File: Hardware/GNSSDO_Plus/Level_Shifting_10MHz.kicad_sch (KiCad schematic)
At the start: 57 parts, among them J10 SMA_Edge, J8 SMA_Edge, U15 SN74LVC1G175DCK, U17 LMV7219M5, U20 LMV7219M5, U23 LMV7219M5, U24 LMV7219M5

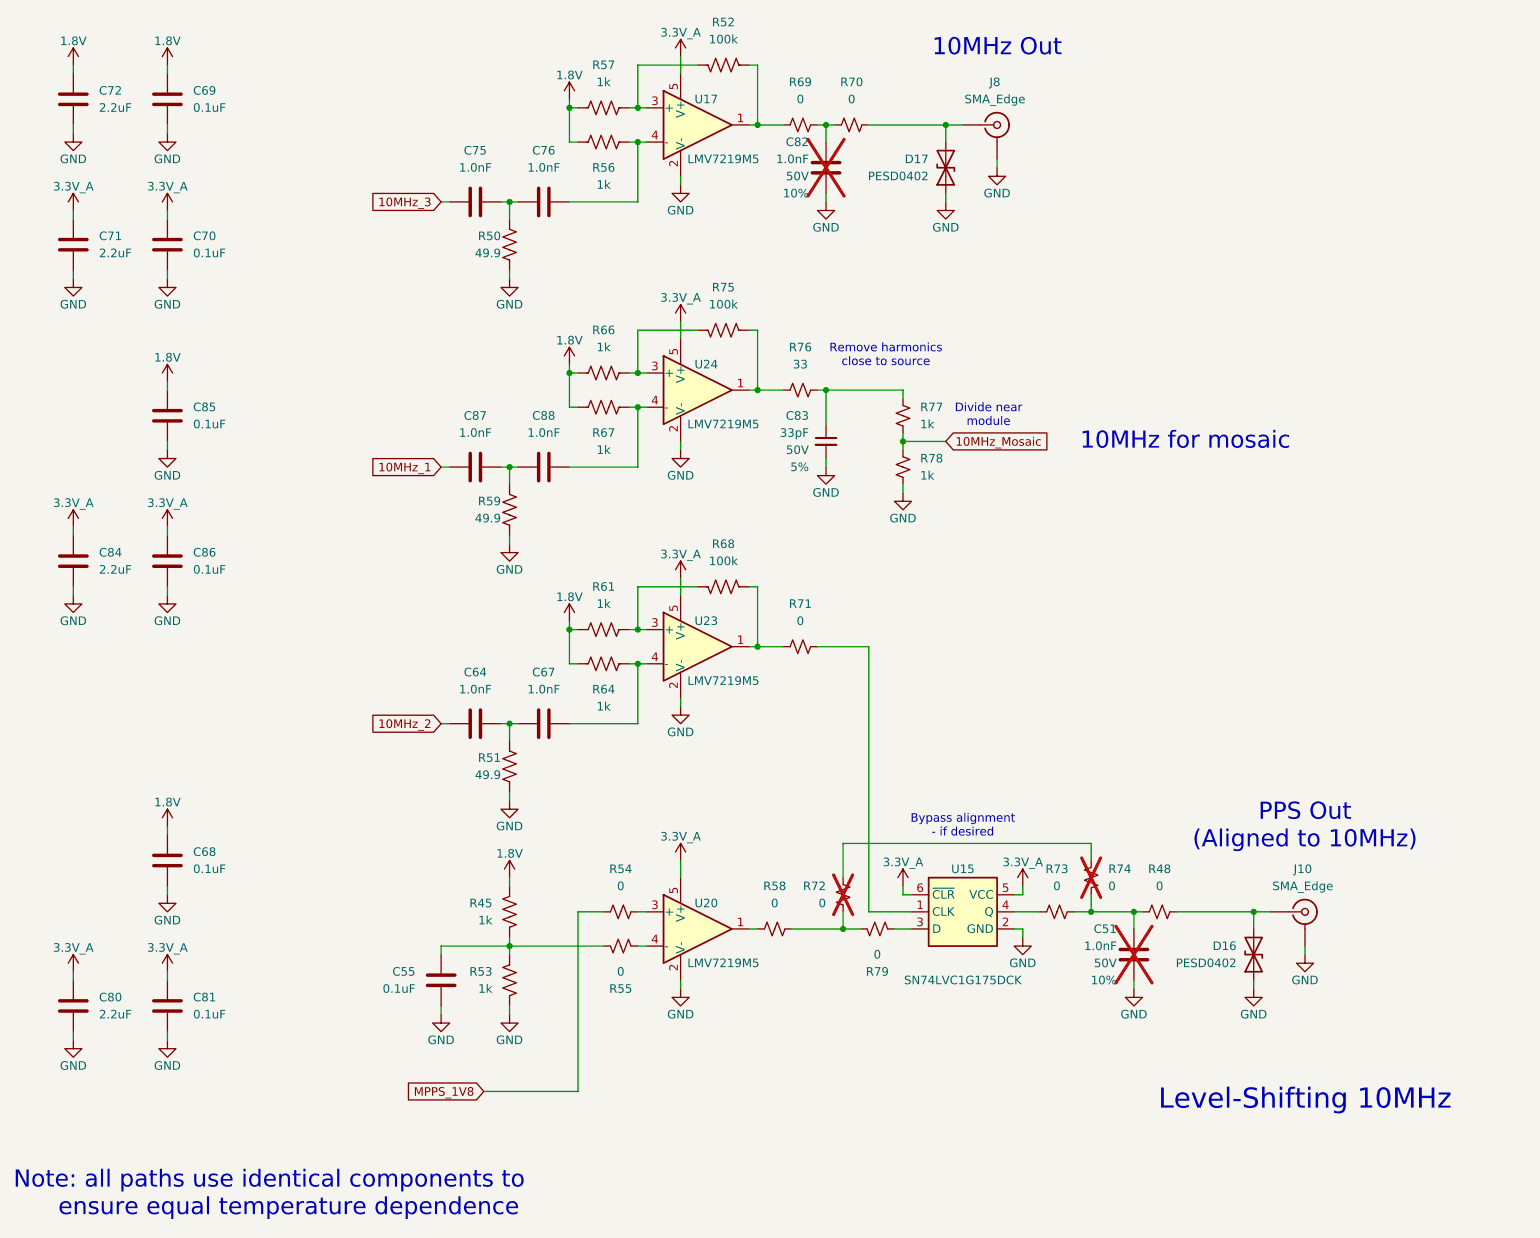
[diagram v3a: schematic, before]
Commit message: GNSSDO+ : update symbols and footprints
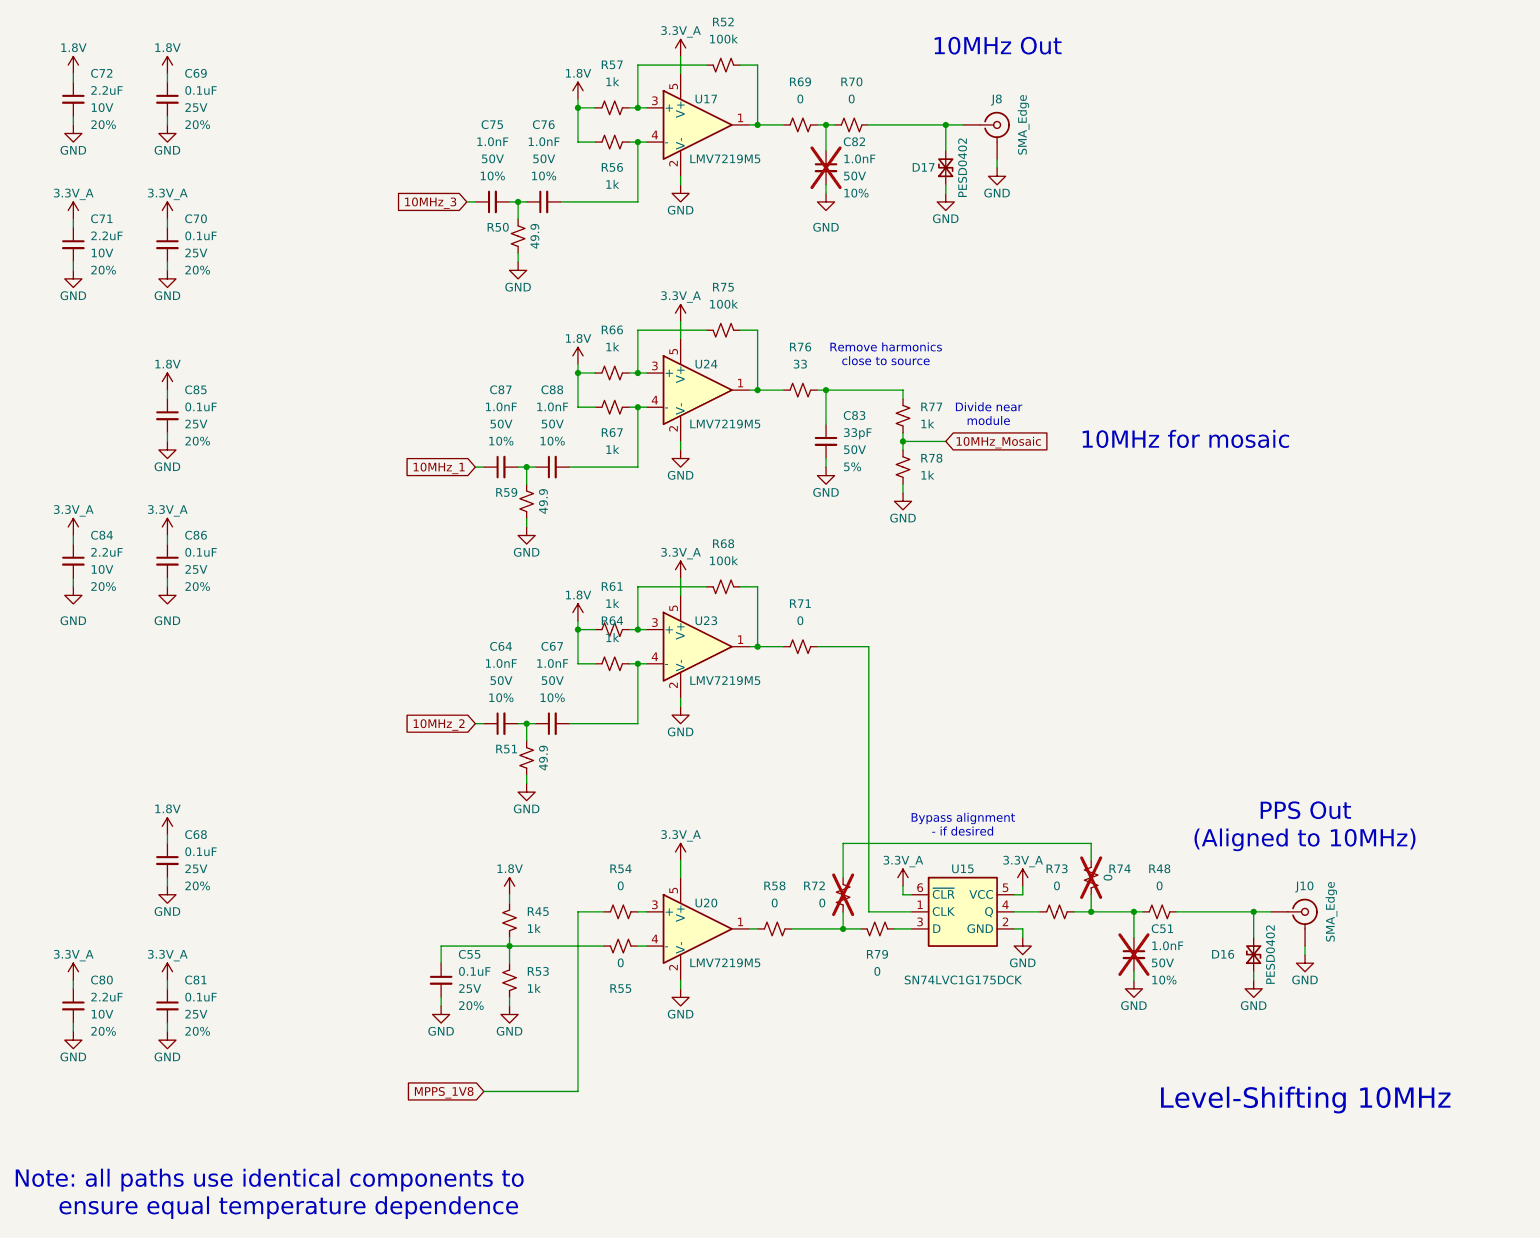
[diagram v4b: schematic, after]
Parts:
- C51, C82, R72, R74: now in the parts list
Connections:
- net 1.8V: now also R45.1, R56.2, R57.2, R61.2, R64.2, R66.2, R67.2; no longer R45.2, R56.1, R57.1, R61.1, R64.1, R66.1, R67.1
- net GND: now also R50.2, R51.2, R53.2, R59.2; no longer R50.1, R51.1, R53.1, R59.1
- net at R69.1, U17.1: now also R52.2; no longer R52.1
- net at C64.2, C67.1: now also R51.1; no longer R51.2
- net at C87.2, C88.1: now also R59.1; no longer R59.2
- net at C88.2, U24.4 (-): now also R67.1; no longer R67.2
- net at C55.1, R55.1: now also R45.2, R53.1; no longer R45.1, R53.2
- net at R76.1, U24.1: now also R75.2; no longer R75.1
- net at R71.1, U23.1: now also R68.2; no longer R68.1
- net at C75.2, C76.1: now also R50.1; no longer R50.2
- net at C67.2, U23.4 (-): now also R64.1; no longer R64.2
- net at C76.2, U17.4 (-): now also R56.1; no longer R56.2
- new net: R52.1, R57.1, U17.3 (+)
- new net: R66.1, R75.1, U24.3 (+)
- new net: R61.1, R68.1, U23.3 (+)
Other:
- moved on the sheet: C64, C67, C75, C87, C88

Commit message: GNSSDO Plus - ready for review
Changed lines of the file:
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@@
 		(on_board yes)
 		(dnp no)
+		(fields_autoplaced yes)
 		(property "Reference" "R51"
-			(at 95.25 127 90)
-			(effects
-				(font
-					(size 1.27 1.27)
-				)
-				(justify right)
+			(at 99.06 126.9999 90)
+			(effects
+				(font
+					(size 1.27 1.27)
+				)
+				(justify left)
 			)
 		)
 		(property "Value" "49.9"
-			(at 99.06 128.27 0)
-			(effects
-				(font
-					(size 1.27 1.27)
-				)
+			(at 99.06 129.5399 90)
+			(effects
+				(font
+					(size 1.27 1.27)
+				)
+				(justify left)
 			)
 		)
@@
 		(on_board yes)
 		(dnp no)
+		(fields_autoplaced yes)
 		(property "Reference" "R59"
-			(at 95.25 88.9 90)
-			(effects
-				(font
-					(size 1.27 1.27)
-				)
-				(justify right)
+			(at 99.06 88.8999 90)
+			(effects
+				(font
+					(size 1.27 1.27)
+				)
+				(justify left)
 			)
 		)
 		(property "Value" "49.9"
-			(at 99.06 90.17 0)
-			(effects
-				(font
-					(size 1.27 1.27)
-				)
+			(at 99.06 91.4399 90)
+			(effects
+				(font
+					(size 1.27 1.27)
+				)
+				(justify left)
 			)
 		)
@@
 		(on_board yes)
 		(dnp no)
+		(fields_autoplaced yes)
 		(property "Reference" "R50"
-			(at 93.98 49.53 90)
-			(effects
-				(font
-					(size 1.27 1.27)
-				)
-				(justify right)
+			(at 97.79 49.5299 90)
+			(effects
+				(font
+					(size 1.27 1.27)
+				)
+				(justify left)
 			)
 		)
 		(property "Value" "49.9"
-			(at 97.79 50.8 0)
-			(effects
-				(font
-					(size 1.27 1.27)
-				)
+			(at 97.79 52.0699 90)
+			(effects
+				(font
+					(size 1.27 1.27)
+				)
+				(justify left)
 			)
 		)
@@
 		(fields_autoplaced yes)
 		(property "Reference" "R64"
-			(at 109.22 107.95 0)
+			(at 109.22 118.11 0)
 			(effects
 				(font
@@
 		)
 		(property "Value" "1k"
-			(at 109.22 110.49 0)
-			(effects
-				(font
+			(at 109.22 120.65 0)
+			(effects
+				(font

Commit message: GNSSDO+ PCB ready for protos
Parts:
- added TP46, TP47: 1.25mm, SparkFun-Connector:TestPoint-1.25mm, symbol SparkFun-Connector:TestPoint_1.25mm
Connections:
- net at D16.2 (A2), J10.1 (In), R48.2: now also TP46.1
- net at D17.2 (A2), J8.1 (In), R70.2: now also TP47.1
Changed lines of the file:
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@@
 	(wire
 		(pts
+			(xy 204.47 149.86) (xy 204.47 151.13)
+		)
+		(stroke
+			(width 0)
+			(type default)
+		)
+	)
+	(wire
+		(pts
 			(xy 104.14 109.22) (xy 106.68 109.22)
 		)
@@
 	(wire
 		(pts
+			(xy 158.75 33.02) (xy 158.75 34.29)
+		)
+		(stroke
+			(width 0)
+			(type default)
+		)
+	)
+	(wire
+		(pts
 			(xy 152.4 87.63) (xy 152.4 88.9)
 		)
@@
 	)
 	(symbol
+		(lib_id "SparkFun-Connector:TestPoint_1.25mm")
+		(at 158.75 33.02 0)
+		(unit 1)
+		(exclude_from_sim no)
+		(in_bom yes)
+		(on_board yes)
+		(dnp no)
+		(fields_autoplaced yes)
+		(property "Reference" "TP47"
+			(at 158.75 27.94 0)
+			(do_not_autoplace yes)
+			(effects
+				(font
+					(size 1.27 1.27)
+				)
+			)
+		)
+		(property "Value" "1.25mm"
+			(at 158.75 36.83 0)
+			(effects
+				(font
+					(size 1.27 1.27)
+				)
+				(hide yes)
+			)
+		)
+		(property "Footprint" "SparkFun-Connector:TestPoint-1.25mm"
+			(at 158.75 39.37 0)
+			(effects
+				(font
+					(size 1.27 1.27)
+				)
+				(hide yes)
+			)
+		)
+		(property "Datasheet" "~"
+			(at 158.75 40.64 0)
+			(effects
+				(font
+					(size 1.27 1.27)
+				)
+				(hide yes)
+			)
+		)
+		(property "Description" "Test Point"
+			(at 158.75 43.18 0)
+			(effects
+				(font
+					(size 1.27 1.27)
+				)
+				(hide yes)
+			)
+		)
+		(pin "1"
+		)
+		(instances
+			(project ""
+				(path "/e3dd3ae4-244d-4cba-9cca-5d2abf83f29a/e788e229-99ae-40ff-993c-e79a627e85af"
+					(reference "TP47")
+					(unit 1)
+				)
+			)
+		)
+	)
+	(symbol
 		(lib_id "SparkFun-PowerSymbol:GND")
 		(at 119.38 120.65 0)
@@
 					(unit 1)
 				)
+			)
+		)
+	)
+	(symbol
+		(lib_id "SparkFun-Connector:TestPoint_1.25mm")
+		(at 204.47 149.86 0)
+		(unit 1)
+		(exclude_from_sim no)
+		(in_bom yes)
+		(on_board yes)
+		(dnp no)
+		(fields_autoplaced yes)
+		(property "Reference" "TP46"
+			(at 204.47 144.78 0)
+			(do_not_autoplace yes)
+			(effects
+				(font
+					(size 1.27 1.27)
+				)
+			)
+		)
+		(property "Value" "1.25mm"
+			(at 204.47 153.67 0)
+			(effects
+				(font
+					(size 1.27 1.27)
+				)
+				(hide yes)
+			)
+		)
+		(property "Footprint" "SparkFun-Connector:TestPoint-1.25mm"
+			(at 204.47 156.21 0)
+			(effects
+				(font
+					(size 1.27 1.27)
+				)
+				(hide yes)
+			)
+		)
+		(property "Datasheet" "~"
+			(at 204.47 157.48 0)
+			(effects
+				(font
+					(size 1.27 1.27)
+				)
+				(hide yes)
+			)
+		)
+		(property "Description" "Test Point"
+			(at 204.47 160.02 0)
+			(effects
+				(font
+					(size 1.27 1.27)
+				)
+				(hide yes)
+			)
+		)
+		(pin "1"
+		)
+		(instances
+			(project ""
+				(path "/e3dd3ae4-244d-4cba-9cca-5d2abf83f29a/e788e229-99ae-40ff-993c-e79a627e85af"
+					(reference "TP46")
+					(unit 1)
+				)

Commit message: GNSSDO+ v02 PCB - with DP5305 PoE module, PowerPath Controllers and MS8607 PHT sensor
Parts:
- D16, D17: symbol SparkFun-DiscreteSemi:D_TVS_0402 -> SparkFun-DiscreteSemi:D_TVS_0402_14V; Rating (none) -> 14VWM/40VC
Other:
- title: Level Shifting 10MHz -> GNSSDO Plus - Level Shifting 10MHz
